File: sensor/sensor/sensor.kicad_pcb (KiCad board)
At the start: 2 copper layers, 72.2 x 21 mm, 59 parts, among them IC1 VL53L4CDV0DH_1, IC2 ISL29125IROZ-T7, J1 RJ12_Shielded, J2 Conn_01x04, J3 Conn_01x06, J8 RJ12_Shielded, J9 Conn_01x06, SW5 SW_Coded_SH-7050, U1 PCA9615DP, U2 LTC4316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

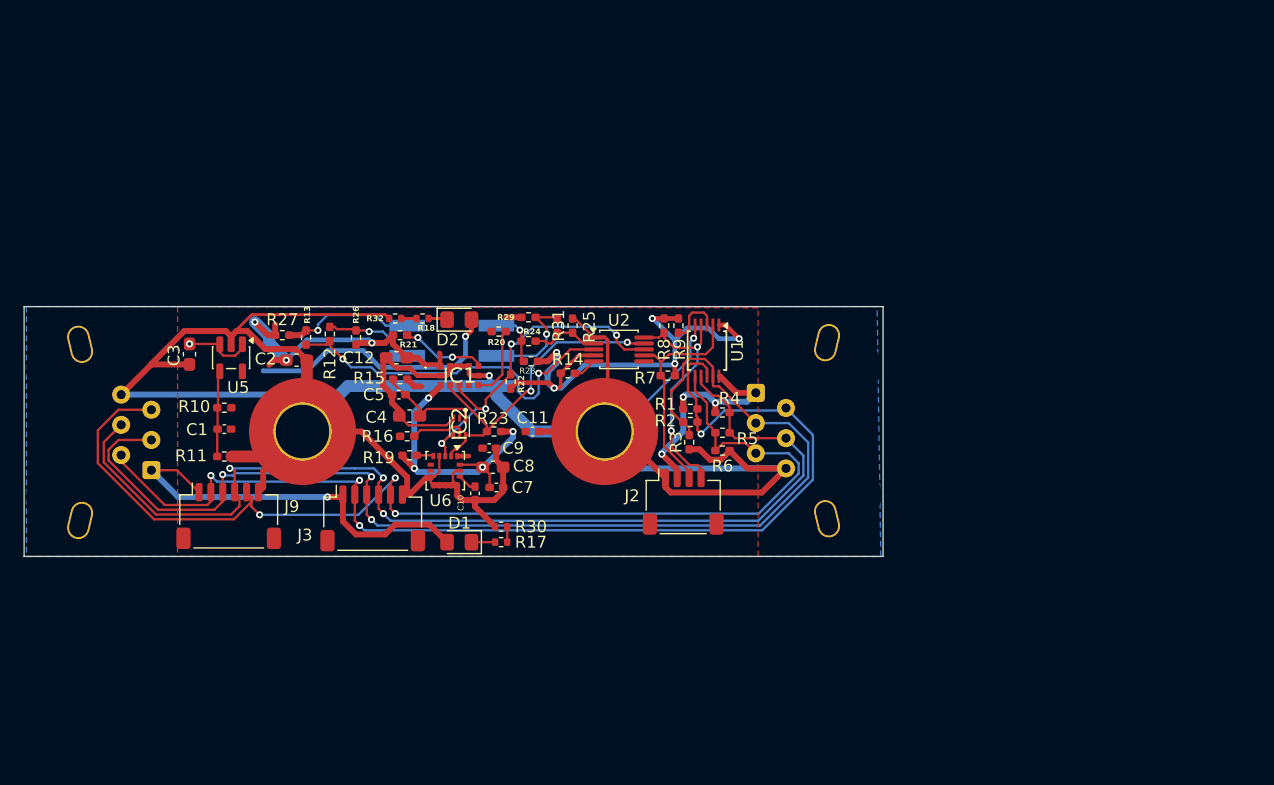
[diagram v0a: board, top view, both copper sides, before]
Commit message: minimizing sensor main board
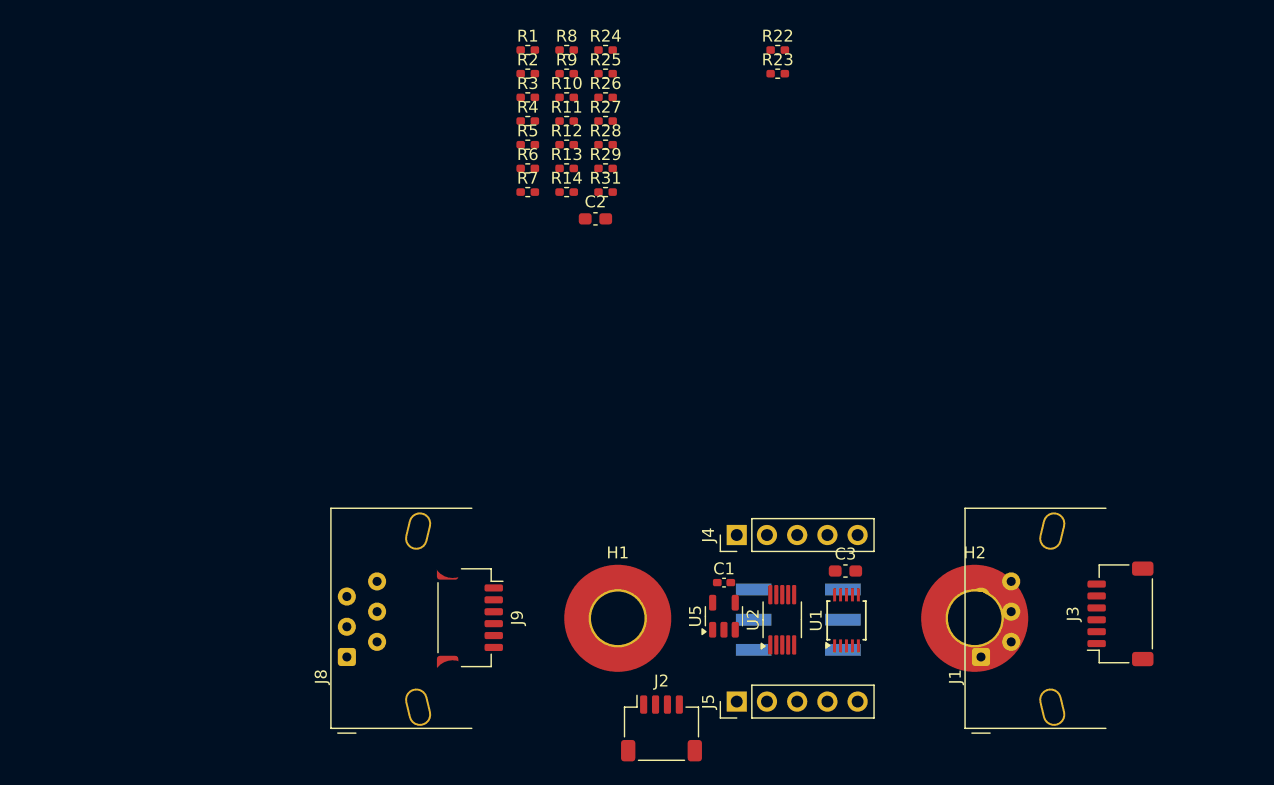
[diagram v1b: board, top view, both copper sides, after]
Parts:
- removed C10, C11, C5, C7: 0.1u, Capacitor_SMD:C_0402_1005Metric_Pad0.74x0.62mm_HandSolder
- removed C12: 4.7u, Capacitor_SMD:C_0603_1608Metric_Pad1.08x0.95mm_HandSolder
- removed C4: 1u, Capacitor_SMD:C_0603_1608Metric_Pad1.08x0.95mm_HandSolder
- removed C8: 2.2u, Capacitor_SMD:C_0603_1608Metric_Pad1.08x0.95mm_HandSolder
- removed C9: 10n, Capacitor_SMD:C_0402_1005Metric_Pad0.74x0.62mm_HandSolder
- removed D1, D2: WHITE, LED_SMD:LED_0805_2012Metric_Pad1.15x1.40mm_HandSolder
- removed IC1: VL53L4CDV0DH_1, VL53L4CD:VL53L4CDV0DH1
- removed IC2: ISL29125IROZ-T7, ISL29125:ISL29125IROZT7
- removed R15: 100, Resistor_SMD:R_0402_1005Metric_Pad0.72x0.64mm_HandSolder
- removed R16, R19: 4.7k, Resistor_SMD:R_0402_1005Metric_Pad0.72x0.64mm_HandSolder
- removed R17, R18, R30, R32: 120, Resistor_SMD:R_0402_1005Metric
- removed R20, R21: 10k, Resistor_SMD:R_0402_1005Metric_Pad0.72x0.64mm_HandSolder
- removed U6: ICM-20602, Package_LGA:LGA-16_3x3mm_P0.5mm_LayoutBorder3x5y
- added J4: Conn_01x05, Connector_PinHeader_2.54mm:PinHeader_1x05_P2.54mm_Vertical, F.Cu at (125.0, 103.0)
- added J5: Conn_01x05, Connector_PinHeader_2.54mm:PinHeader_1x05_P2.54mm_Vertical, F.Cu at (125.0, 117.0)
- J1, J8: moved to F.Cu
- moved J1 71.5 mm to (145.5, 113.2)
- moved J3 63.4 mm to (157.2, 109.6), turned to 90 degrees
- moved C3 58.1 mm to (134.1, 106.0), turned to 0 degrees
- moved U5 46.8 mm to (123.9, 109.8), turned to 90 degrees
- moved C1 43.9 mm to (123.9, 107.0), turned to 0 degrees
- moved J8 40.9 mm to (92.2, 113.2), turned to 90 degrees
- moved R11 40.3 mm to (110.7, 68.2)
- moved R10 38.8 mm to (110.7, 66.2), turned to 0 degrees
- moved R23 38.4 mm to (128.4, 64.2), turned to 0 degrees
- moved R22 35.8 mm to (128.4, 62.2), turned to 0 degrees
- moved H2 34.8 mm to (145.0, 110.0)
- moved R1 33.1 mm to (107.4, 62.2)
- moved R27 32.6 mm to (114.0, 68.2)
- moved R2 32.3 mm to (107.4, 64.2)
- moved R3 32.0 mm to (107.4, 66.2), turned to 0 degrees
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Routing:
- net GND: track 236.8 -> 0.00 mm, vias 2 -> 0
- net Net-(J3-Pin_3): track 98.5 -> 0.00 mm, vias 3 -> 0
- net +3.3V: track 97.1 -> 0.00 mm, vias 12 -> 0
- net Net-(J3-Pin_5): track 93.3 -> 0.00 mm, vias 3 -> 0
- net Net-(J3-Pin_2): track 92.6 -> 0.00 mm, vias 4 -> 0
- net Net-(J3-Pin_4): track 89.3 -> 0.00 mm, vias 3 -> 0
- net +5V: track 82.4 -> 0.00 mm, vias 6 -> 0
- net Net-(U2-XORL): track 30.4 -> 0.00 mm, vias 2 -> 0
- net /Sensors/sda: track 29.9 -> 0.00 mm, vias 4 -> 0
- net /Sensors/scl: track 27.0 -> 0.00 mm, vias 2 -> 0
- net Net-(J2-Pin_4): track 20.8 -> 0.00 mm, vias 2 -> 0
- net Net-(J2-Pin_3): track 19.3 -> 0.00 mm
- net Net-(R13-Pad1): track 11.3 -> 0.00 mm, vias 1 -> 0
- net Net-(R25-Pad1): track 9.18 -> 0.00 mm, vias 1 -> 0
- net Net-(IC2-VDD): track 8.97 -> 0.00 mm
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- removed copper zone on F.Cu, net +3.3V
- removed copper zone on B.Cu, net +5V
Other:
- board outline removed

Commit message: finished main sensor board
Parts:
- removed J8: RJ12_Shielded, RJ12_Pin_Connector:RJ12_Pin_Connector
- removed U2: LTC4316, Package_SO:MSOP-10_3x3mm_P0.5mm
- added G***: LOGO, LOGO, F.Cu at (110.3, 105.6)
- added G***: LOGO, LOGO, B.Cu at (110.7, 102.8)
- added G***: LOGO, LOGO, B.Cu at (114.8, 101.9)
- added IC1: LTC4316CMS#TRPBF, LTC4316CMS:SOP50P490X110-10N, F.Cu at (135.1, 109.5)
- added J6: GDLX-SMT-N-66, GDLX-SMT-N-66:GDLXSMTN66, B.Cu at (107.9, 109.0)
- J1: value RJ12_Shielded -> GDLX-SMT-N-66; footprint RJ12_Pin_Connector:RJ12_Pin_Connector -> GDLX-SMT-N-66:GDLXSMTN66; moved to B.Cu
- moved R8 59.4 mm to (140.1, 113.9), turned to 180 degrees
- moved R9 56.5 mm to (137.7, 113.9), turned to 180 degrees
- moved R3 56.2 mm to (149.9, 103.1)
- moved R2 55.8 mm to (147.4, 103.1), turned to 180 degrees
- moved R1 55.4 mm to (144.9, 103.1)
- moved R24 53.4 mm to (127.5, 114.0)
- moved R7 53.0 mm to (142.6, 113.9)
- moved R25 52.6 mm to (127.4, 115.0)
- moved R26 51.7 mm to (121.8, 117.3)
- moved R12 50.0 mm to (127.4, 117.3)
- moved R4 49.2 mm to (143.9, 101.2), turned to -90 degrees
- moved R6 49.1 mm to (147.0, 101.2), turned to -90 degrees
- moved R5 48.9 mm to (145.2, 101.2), turned to -90 degrees
- moved R27 48.6 mm to (121.7, 116.2)
- moved R13 47.1 mm to (127.4, 116.2)
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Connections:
- R14 pad 1: +3.3V -> Net-(IC1-ENABLE)
- R14 pad 2: Net-(U2-ENABLE) -> +3.3V
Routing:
- net GND: track 0.00 -> 137.8 mm, vias 0 -> 6
- net +3.3V: track 0.00 -> 85.2 mm, vias 0 -> 7
- net Net-(J3-Pin_5): track 0.00 -> 83.5 mm, vias 0 -> 4
- net Net-(J3-Pin_4): track 0.00 -> 79.9 mm, vias 0 -> 4
- net +5V: track 0.00 -> 79.6 mm, vias 0 -> 7
- net Net-(J3-Pin_3): track 0.00 -> 78.3 mm, vias 0 -> 4
- net Net-(J3-Pin_2): track 0.00 -> 71.6 mm, vias 0 -> 4
- net Net-(IC1-SDAIN): track 0.00 -> 38.5 mm, vias 0 -> 2
- net Net-(IC1-SCLIN): track 0.00 -> 37.3 mm, vias 0 -> 4
- net Net-(R25-Pad1): track 0.00 -> 24.0 mm, vias 0 -> 1
- net Net-(R24-Pad1): track 0.00 -> 23.9 mm, vias 0 -> 1
- net /Sensors/sda: track 0.00 -> 23.1 mm, vias 0 -> 3
- net /Sensors/scl: track 0.00 -> 20.9 mm, vias 0 -> 3
- net Net-(R13-Pad1): track 0.00 -> 19.6 mm, vias 0 -> 1
- net Net-(R12-Pad1): track 0.00 -> 16.8 mm, vias 0 -> 1
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- added copper zone on B.Cu, net +5V
- added copper zone on F.Cu, net GND
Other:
- board outline added: 66.1 x 19 mm
- board text added: "ALLEN A KARMA. M ANDREW K JENNY C"
- board text added: "IEEE RAS VEXU GHOST SENSOR BOARD"
